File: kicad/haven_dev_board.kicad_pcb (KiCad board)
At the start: 6 copper layers, 72.9 x 160.9 mm, 89 parts, among them CN1 BM46B-12DS-0.35V(51).1, J1 CLE-107-01-G-DV.1, Q1 CSD23382F4.1, Q2 CSD13380F3T.1, Q3 CSD13380F3T.1, SW1 TS2819A 230GF.1, U1 BMX160.1, U10 SN74AXC4T774RSVR.1, U12 GT-USB-9047A.1, U13 SPH0641LU4H-1.1, U14 MX25R6435FBFIL0.1, U15 ADAU1860BCBZRL.1, U2 BQ25120AYFPR.1, U3 AP22916BCA4-7.1, U4 XL-0201SURC.1, U5 KTD2026.1, U6 BQ27220YZFR.1, U8 1MΩ.1, U9 AP22916BCA4-7.1, X1 Q13FC1350000200.1

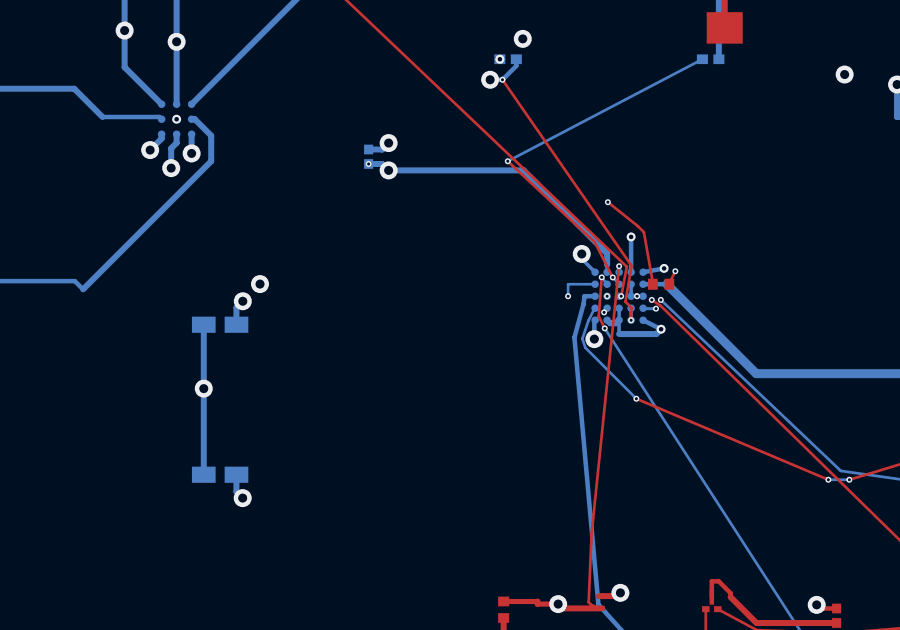
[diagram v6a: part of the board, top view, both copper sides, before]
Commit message: Move C16 (V_PMID 4.7 uF) next to U2; DRC 219 -> 219, 0 new
Was 13.3 mm from the charger's V_PMID balls (A3/B3/B4). Same method as C22
(via-stitch onto the rail's inner-layer run outside the escape field, GND
on its own via, old feed's dangling remnants removed).

kicad-cli 9.0.8: 219 violations / 2 unconnected before and after.

Co-Authored-By: Claude Fable 5.1 <noreply@anthropic.com>
Claude-Session: https://claude.ai/code/session_01K7G9Bv5agmyedmt776NSLV
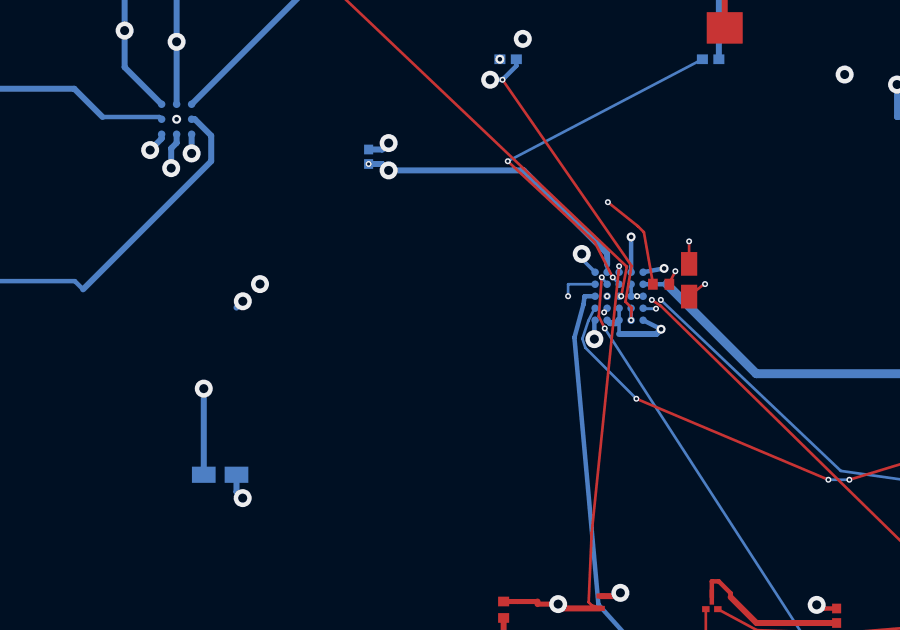
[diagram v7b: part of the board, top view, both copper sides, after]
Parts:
- C16: moved to F.Cu
- moved C16 15.7 mm to (68.8, 32.3), turned to -90 degrees
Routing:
- net GND: track 662.7 -> 661.4 mm, vias 66 -> 67
- net V_PMID: track 32.2 -> 32.3 mm, vias 4 -> 5
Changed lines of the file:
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@@
 		(embedded_fonts no)
 	)
+	(footprint "haven_footprints:C0402"
+		(layer "F.Cu")
+		(at 68.843 32.344 -90)
+		(property "Reference" "C16"
+			(at 0 1.5 90)
+			(layer "F.SilkS")
+			(hide yes)
+			(effects
+				(font
+					(size 0.8 0.8)
+					(thickness 0.12)
+				)
+				(justify mirror)
+			)
+		)
+		(property "Value" "4.7uF, 10V.1"
+			(at 0 -1.5 90)
+			(layer "F.Fab")
+			(hide yes)
+			(effects
+				(font
+					(size 0.8 0.8)
+					(thickness 0.12)
+				)
+				(justify mirror)
+			)
+		)
+		(property "Datasheet" ""
+			(at 0 0 90)
+			(layer "B.Fab")
+			(hide yes)
+			(effects
+				(font
+					(size 1.27 1.27)
+					(thickness 0.15)
+				)
+				(justify mirror)
+			)
+		)
+		(property "Description" ""
+			(at 0 0 90)
+			(layer "B.Fab")
+			(hide yes)
+			(effects
+				(font
+					(size 1.27 1.27)
+					(thickness 0.15)
+				)
+				(justify mirror)
+			)
+		)
+		(attr smd)
+		(pad "1" smd rect
+			(at -0.545 0 270)
+			(size 0.7901 0.54)
+			(layers "F.Cu" "F.Mask" "F.Paste")
+			(net 25 "GND")
+		)
+		(pad "2" smd rect
+			(at 0.5451 0 270)
+			(size 0.7901 0.54)
+			(layers "F.Cu" "F.Mask" "F.Paste")
+			(net 79 "V_PMID")
+		)
+		(embedded_fonts no)
+	)
 	(footprint "haven_footprints:C0201"
 		(layer "F.Cu")
@@
 		(embedded_fonts no)
 	)
-	(footprint "haven_footprints:C0402"
-		(layer "B.Cu")
-		(at 53.2103 33.8277)
-		(property "Reference" "C16"
-			(at 0 -1.5 0)
-			(layer "B.SilkS")
-			(hide yes)
-			(effects
-				(font
-					(size 0.8 0.8)
-					(thickness 0.12)
-				)
-			)
-		)
-		(property "Value" "4.7uF, 10V.1"
-			(at 0 1.5 0)
-			(layer "B.Fab")
-			(hide yes)
-			(effects
-				(font
-					(size 0.8 0.8)
-					(thickness 0.12)
-				)
-			)
-		)
-		(property "Datasheet" ""
-			(at 0 0 0)
-			(layer "F.Fab")
-			(hide yes)
-			(effects
-				(font
-					(size 1.27 1.27)
-					(thickness 0.15)
-				)
-			)
-		)
-		(property "Description" ""
-			(at 0 0 0)
-			(layer "F.Fab")
-			(hide yes)
-			(effects
-				(font
-					(size 1.27 1.27)
-					(thickness 0.15)
-				)
-			)
-		)
-		(attr smd)
-		(pad "1" smd rect
-			(at -0.545 0)
-			(size 0.7901 0.54)
-			(layers "B.Cu" "B.Mask" "B.Paste")
-			(net 25 "GND")
-		)
-		(pad "2" smd rect
-			(at 0.5451 0)
-			(size 0.7901 0.54)
-			(layers "B.Cu" "B.Mask" "B.Paste")
-			(net 79 "V_PMID")
-		)
-		(embedded_fonts no)
-	)
 	(footprint "haven_footprints:C0201"
 		(layer "B.Cu")
@@
 	)
 	(segment
+		(start 68.843 31.049)
+		(end 68.843 31.849)
+		(width 0.09)
+		(layer "F.Cu")
+		(net 25)
+	)
+	(segment
 		(start 65.8122 134.9906)
 		(end 65.6644 134.9906)
@@
 	)
 	(via
+		(at 68.843 31.049)
+		(size 0.2)
+		(drill 0.1)
+		(layers "F.Cu" "B.Cu")
+		(net 25)
+	)
+	(via
 		(at 96.5 34.9277)
 		(size 0.3)
@@
 	)
 	(segment
-		(start 52.6653 33.8277)
-		(end 52.6653 35.9566)
-		(width 0.2)
-		(locked yes)
-		(layer "B.Cu")
-		(net 25)
-	)
-	(segment
 		(start 78.905 127.7968)
 		(end 78.6524 127.7968)
@@
 		(net 78)
 	)
+	(segment
+		(start 69.343 32.472)
+		(end 68.843 32.872)
+		(width 0.09)
+		(layer "F.Cu")
+		(net 79)
+	)
+	(via
+		(at 69.374818 32.472)
+		(size 0.2)
+		(drill 0.1)
+		(layers "F.Cu" "B.Cu")
+		(net 79)
+	)
 	(via
 		(at 67.109 32.8772)
@@
 		(locked yes)
 		(layer "B.Cu")
-		(net 79)
-	)
-	(segment
-		(start 53.7554 33.8277)
-		(end 53.7554 33.256)
-		(width 0.2)
-		(locked yes)
-		(layer "B.Cu")

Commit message: Move C18 (+1.8V 10 uF) next to U2 ball B5; DRC 219 -> 219, 0 new
Was 12.7 mm from the charger's +1.8V output ball; now on B.Cu 1.0 mm from
it. The old feed still serves L2's +1.8V pad so nothing dangled; the first
candidate was rejected by the tool's own final via re-check (a new via
0.19 mm from copper) before it ever reached DRC.

kicad-cli 9.0.8: 219 violations / 2 unconnected before and after.

Co-Authored-By: Claude Fable 5.1 <noreply@anthropic.com>
Claude-Session: https://claude.ai/code/session_01K7G9Bv5agmyedmt776NSLV
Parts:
- moved C18 12.4 mm to (66.7, 31.1)
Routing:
- net GND: track 661.4 -> 662.0 mm, vias 67 -> 68
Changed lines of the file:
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@@
 	(footprint "haven_footprints:C0402"
 		(layer "B.Cu")
-		(at 79.1403 31.5387)
+		(at 66.709999 31.077)
 		(property "Reference" "C18"
 			(at 0 -1.5 0)
@@
 	)
 	(segment
+		(start 66.9098 30.9)
+		(end 67.2098 31.099999)
+		(width 0.09)
+		(layer "B.Cu")
+		(net 14)
+	)
+	(segment
 		(start 53.9625 39.6065)
 		(end 53.7554 39.3994)
@@
 	)
 	(via
+		(at 66.373012 30.437)
+		(size 0.2)
+		(drill 0.1)
+		(layers "F.Cu" "B.Cu")
+		(net 25)
+	)
+	(via
 		(at 105.559851 110.963931)
 		(size 0.2)
@@
 		(layer "B.Cu")
 		(net 25)
+	)
+	(segment
+		(start 66.364899 30.437)
+		(end 66.164899 31.037)
+		(width 0.09)
+		(layer "B.Cu")
+		(net 25)
